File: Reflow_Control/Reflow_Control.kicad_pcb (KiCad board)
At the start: 2 copper layers, 100 x 80 mm, 71 parts, among them J1 Conn_5V, J2 Conn_ssr_1, J3 Conn_ssr_2, J4 Conn_mot_PWR, J5 Conn_mot_1, J6 Conn_mot_2, Q1 NUD3112LT1G, Q2 NUD3112LT1G, Q3 BC848, SW1 SW_Push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

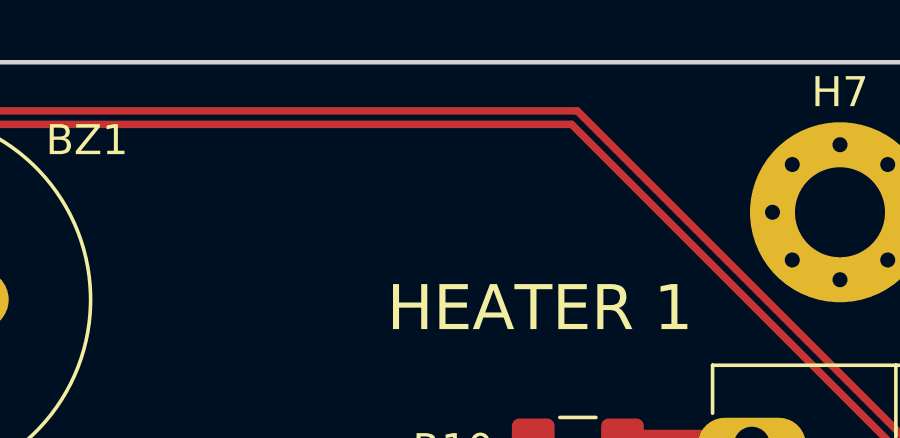
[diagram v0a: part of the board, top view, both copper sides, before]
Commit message: changed part attributes
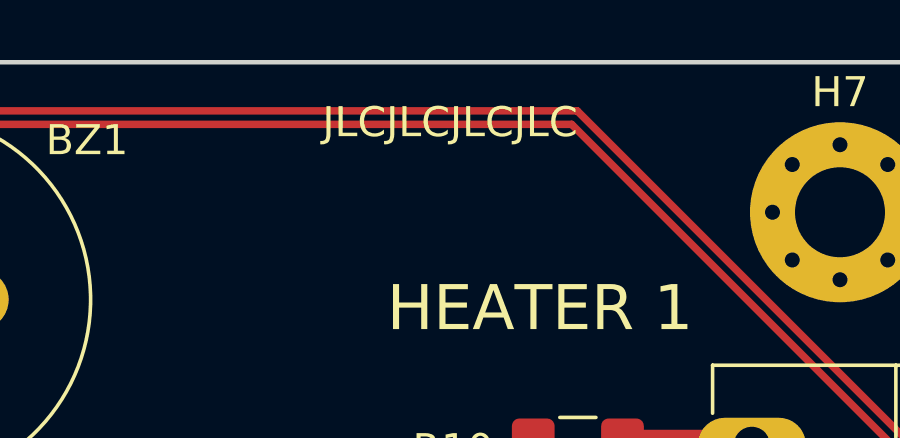
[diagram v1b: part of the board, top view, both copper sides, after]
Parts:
- Q1: value NUD3112LT1G -> Q_NMOS_GSD
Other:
- board text added: "JLCJLCJLCJLC"
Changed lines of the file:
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@@
   (general
     (thickness 1.6)
-    (drawings 13)
+    (drawings 12)
     (tracks 449)
     (zones 0)
@@
     (38 B.Mask user hide)
     (39 F.Mask user hide)
-    (40 Dwgs.User user hide)
+    (40 Dwgs.User user)
     (41 Cmts.User user hide)
     (42 Eco1.User user hide)
@@
       (effects (font (size 1 1) (thickness 0.15)))
     )
-    (fp_text value NUD3112LT1G (at 0 2.5) (layer F.Fab)
+    (fp_text value Q_NMOS_GSD (at 0 2.5) (layer F.Fab)
       (effects (font (size 1 1) (thickness 0.15)))
     )
@@
     )
   )
+  (gr_text JLCJLCJLCJLC (at 182 52) (layer F.SilkS)
+    (effects (font (size 1 1) (thickness 0.2)))
+  )
   (gr_text "Edwin Koch & Kerem Yollu" (at 127 54) (layer F.SilkS)
     (effects (font (size 1 1) (thickness 0.2)))
@@
     (effects (font (size 1 1) (thickness 0.2)))
   )
-  (dimension 80 (width 0.3) (layer B.SilkS)
-    (gr_text "80.000 mm" (at 80.5 90 90) (layer B.SilkS)
-      (effects (font (size 1.5 1.5) (thickness 0.3)))
-    )
-    (feature1 (pts (xy 100 50) (xy 82.013579 50)))
-    (feature2 (pts (xy 100 130) (xy 82.013579 130)))
-    (crossbar (pts (xy 82.6 130) (xy 82.6 50)))
-    (arrow1a (pts (xy 82.6 50) (xy 83.186421 51.126504)))
-    (arrow1b (pts (xy 82.6 50) (xy 82.013579 51.126504)))
-    (arrow2a (pts (xy 82.6 130) (xy 83.186421 128.873496)))
-    (arrow2b (pts (xy 82.6 130) (xy 82.013579 128.873496)))
-  )
-  (dimension 100.00005 (width 0.3) (layer B.SilkS)
-    (gr_text "100.000 mm" (at 150.0106 39.45021 359.9427042) (layer B.SilkS)
-      (effects (font (size 1.5 1.5) (thickness 0.3)))
-    )
-    (feature1 (pts (xy 200 50.1) (xy 200.009086 41.013789)))
-    (feature2 (pts (xy 100 50) (xy 100.009086 40.913789)))
-    (crossbar (pts (xy 100.0085 41.500209) (xy 200.0085 41.600209)))
-    (arrow1a (pts (xy 200.0085 41.600209) (xy 198.88141 42.185503)))
-    (arrow1b (pts (xy 200.0085 41.600209) (xy 198.882583 41.012662)))
-    (arrow2a (pts (xy 100.0085 41.500209) (xy 101.134417 42.087756)))
-    (arrow2b (pts (xy 100.0085 41.500209) (xy 101.13559 40.914915)))
-  )
   (gr_text "Reflow Oven Controller" (at 128 52) (layer F.SilkS)

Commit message: v1.0
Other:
- board text added: "+"
- board text added: "-"
- board text removed: "JLCJLCJLCJLC"
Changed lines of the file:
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@@
   (general
     (thickness 1.6)
-    (drawings 12)
+    (drawings 17)
     (tracks 449)
     (zones 0)
@@
     (tags "resistor handsolder")
     (attr smd)
-    (fp_text reference R3 (at -4.953 0) (layer F.SilkS)
+    (fp_text reference R3 (at 0.0285 -1.931) (layer F.SilkS)
       (effects (font (size 1 1) (thickness 0.15)))
     )
@@
     (tags "Tactile Switch")
     (attr smd)
-    (fp_text reference SW1 (at 0 -4.5) (layer F.SilkS)
+    (fp_text reference SW1 (at 0.5 -4.5) (layer F.SilkS)
       (effects (font (size 1 1) (thickness 0.15)))
     )
@@
       (effects (font (size 1 1) (thickness 0.15)))
     )
-    (fp_text user 1 (at -2.6 0) (layer F.SilkS)
+    (fp_text user 1 (at -2.6 -1.28) (layer F.SilkS)
       (effects (font (size 1 1) (thickness 0.15)))
     )
@@
     (descr "Buzzer, D12.2mm height 6.5mm, https://product.tdk.com/info/en/catalog/datasheets/piezoelectronic_buzzer_ps_en.pdf")
     (tags buzzer)
-    (fp_text reference BZ1 (at 8.61 -5.312) (layer F.SilkS)
+    (fp_text reference BZ1 (at 10.96 -0.162 180) (layer F.SilkS)
       (effects (font (size 1 1) (thickness 0.15)))
     )
@@
     (tags "capacitor handsolder")
     (attr smd)
-    (fp_text reference C5 (at 2.93 0) (layer F.SilkS)
+    (fp_text reference C5 (at 3.497 0) (layer F.SilkS)
       (effects (font (size 1 1) (thickness 0.15)))
     )
@@
     (tags "capacitor handsolder")
     (attr smd)
-    (fp_text reference C7 (at -2.921 0) (layer F.SilkS)
+    (fp_text reference C7 (at -3.262 0) (layer F.SilkS)
       (effects (font (size 1 1) (thickness 0.15)))
     )
@@
     (tags "mounting hole 3mm")
     (attr virtual)
-    (fp_text reference H7 (at 0 -4) (layer F.SilkS)
+    (fp_text reference H7 (at -4 -2.75) (layer F.SilkS)
       (effects (font (size 1 1) (thickness 0.15)))
     )
@@
     (tags "mounting hole 3mm")
     (attr virtual)
-    (fp_text reference H9 (at 0 -4) (layer F.SilkS)
+    (fp_text reference H9 (at 3.5 3) (layer F.SilkS)
       (effects (font (size 1 1) (thickness 0.15)))
     )
@@
     (tags "mounting hole 3mm")
     (attr virtual)
-    (fp_text reference H10 (at 0 -4) (layer F.SilkS)
+    (fp_text reference H10 (at 4.5 2) (layer F.SilkS)
       (effects (font (size 1 1) (thickness 0.15)))
     )
@@
     (descr "Generic Phoenix Contact connector footprint for: MC_1,5/2-G-5.08; number of pins: 02; pin pitch: 5.08mm; Angled || order number: 1836189 8A 320V")
     (tags "phoenix_contact connector MC_01x02_G_5.08mm")
-    (fp_text reference J2 (at 9.03 6.6375 90) (layer F.SilkS)
+    (fp_text reference J2 (at 9.08 6.1875 90) (layer F.SilkS)
       (effects (font (size 1 1) (thickness 0.15)))
     )
@@
     (tags "resistor handsolder")
     (attr smd)
-    (fp_text reference R1 (at -3.556 -0.254 90) (layer F.SilkS)
+    (fp_text reference R1 (at -1.866 2.142 180) (layer F.SilkS)
       (effects (font (size 1 1) (thickness 0.15)))
     )
@@
     (tags "resistor handsolder")
     (attr smd)
-    (fp_text reference R2 (at -3.5925 -0.254 90) (layer F.SilkS)
+    (fp_text reference R2 (at -1.866 -2.068 180) (layer F.SilkS)
       (effects (font (size 1 1) (thickness 0.15)))
     )
@@
     (tags "resistor handsolder")
     (attr smd)
-    (fp_text reference R5 (at -3.25 0.125 180) (layer F.SilkS)
+    (fp_text reference R5 (at -3.5 1.75 180) (layer F.SilkS)
       (effects (font (size 1 1) (thickness 0.15)))
     )
@@
     (tags "resistor handsolder")
     (attr smd)
-    (fp_text reference R6 (at -3.375 0 180) (layer F.SilkS)
+    (fp_text reference R6 (at 0 1.875 270) (layer F.SilkS)
       (effects (font (size 1 1) (thickness 0.15)))
     )
@@
     (tags "Tactile Switch")
     (attr smd)
-    (fp_text reference SW4 (at 1.838 -4.558) (layer F.SilkS)
+    (fp_text reference SW4 (at 1 -5) (layer F.SilkS)
       (effects (font (size 1 1) (thickness 0.15)))
     )
@@
     (descr "Through hole straight pin header, 1x04, 2.54mm pitch, single row")
     (tags "Through hole pin header THT 1x04 2.54mm single row")
-    (fp_text reference U1 (at 0 -2.33 90) (layer F.SilkS)
+    (fp_text reference U1 (at 2.65 4.25 180) (layer F.SilkS)
       (effects (font (size 1 1) (thickness 0.15)))
     )
@@
     (descr "Through hole straight pin header, 1x08, 2.54mm pitch, single row")
     (tags "Through hole pin header THT 1x08 2.54mm single row")
-    (fp_text reference U3 (at 0 -2.33 90) (layer F.SilkS)
+    (fp_text reference U3 (at -3.144 8.498 180) (layer F.SilkS)
       (effects (font (size 1 1) (thickness 0.15)))
     )
@@
     (descr "Generic Phoenix Contact connector footprint for: MC_1,5/2-G-5.08; number of pins: 02; pin pitch: 5.08mm; Angled || order number: 1836189 8A 320V")
     (tags "phoenix_contact connector MC_01x02_G_5.08mm")
-    (fp_text reference J3 (at -4.37 7.0375 90) (layer F.SilkS)
+    (fp_text reference J3 (at -4.37 6.1875 90) (layer F.SilkS)
       (effects (font (size 1 1) (thickness 0.15)))
     )
@@
       (effects (font (size 1 1) (thickness 0.15)))
     )
-    (fp_text user 1 (at -2.6 0) (layer F.SilkS)
+    (fp_text user 1 (at -2.6 -1.582) (layer F.SilkS)
       (effects (font (size 1 1) (thickness 0.15)))
     )
@@
     (fp_line (start 1.4 1) (end -1.4 1) (layer F.SilkS) (width 0.12))
     (fp_line (start -2.05 0.3) (end -2.05 -0.3) (layer F.SilkS) (width 0.12))
-    (fp_text user 1 (at -2.6 0) (layer F.SilkS)
+    (fp_text user 1 (at -2.6 -1.978) (layer F.SilkS)
       (effects (font (size 1 1) (thickness 0.15)))
     )
@@
     (zone_connect 2)
     (attr smd)
-    (fp_text reference C15 (at 5.334 3.048 270) (layer F.SilkS)
+    (fp_text reference C15 (at -2.451 -5.287) (layer F.SilkS)
       (effects (font (size 1 1) (thickness 0.15)))
     )
@@
     )
   )
-  (gr_text JLCJLCJLCJLC (at 182 52) (layer F.SilkS)
-    (effects (font (size 1 1) (thickness 0.2)))
+  (gr_text + (at 189.25 72) (layer F.SilkS)
+    (effects (font (size 1.5 1.5) (thickness 0.3)))
+  )
+  (gr_text + (at 188.75 60.5) (layer F.SilkS)
+    (effects (font (size 1.5 1.5) (thickness 0.3)))
+  )
+  (gr_text - (at 118.75 118) (layer F.SilkS)
+    (effects (font (size 1.5 1.5) (thickness 0.3)))
+  )
+  (gr_text + (at 113.5 118) (layer F.SilkS)
+    (effects (font (size 1.5 1.5) (thickness 0.3)))
+  )
+  (gr_text + (at 112 104) (layer F.SilkS)
+    (effects (font (size 1.5 1.5) (thickness 0.3)))
+  )
+  (gr_text + (at 112 92.5) (layer F.SilkS)
+    (effects (font (size 1.5 1.5) (thickness 0.3)))
   )
   (gr_text "Edwin Koch & Kerem Yollu" (at 127 54) (layer F.SilkS)
